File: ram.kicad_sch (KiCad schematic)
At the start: 24 parts, among them U16 SIMM, U17 74LS08, U18 74LS74, U19 74F00, U32 74LS139, U34 74LS244, U35 74LS244

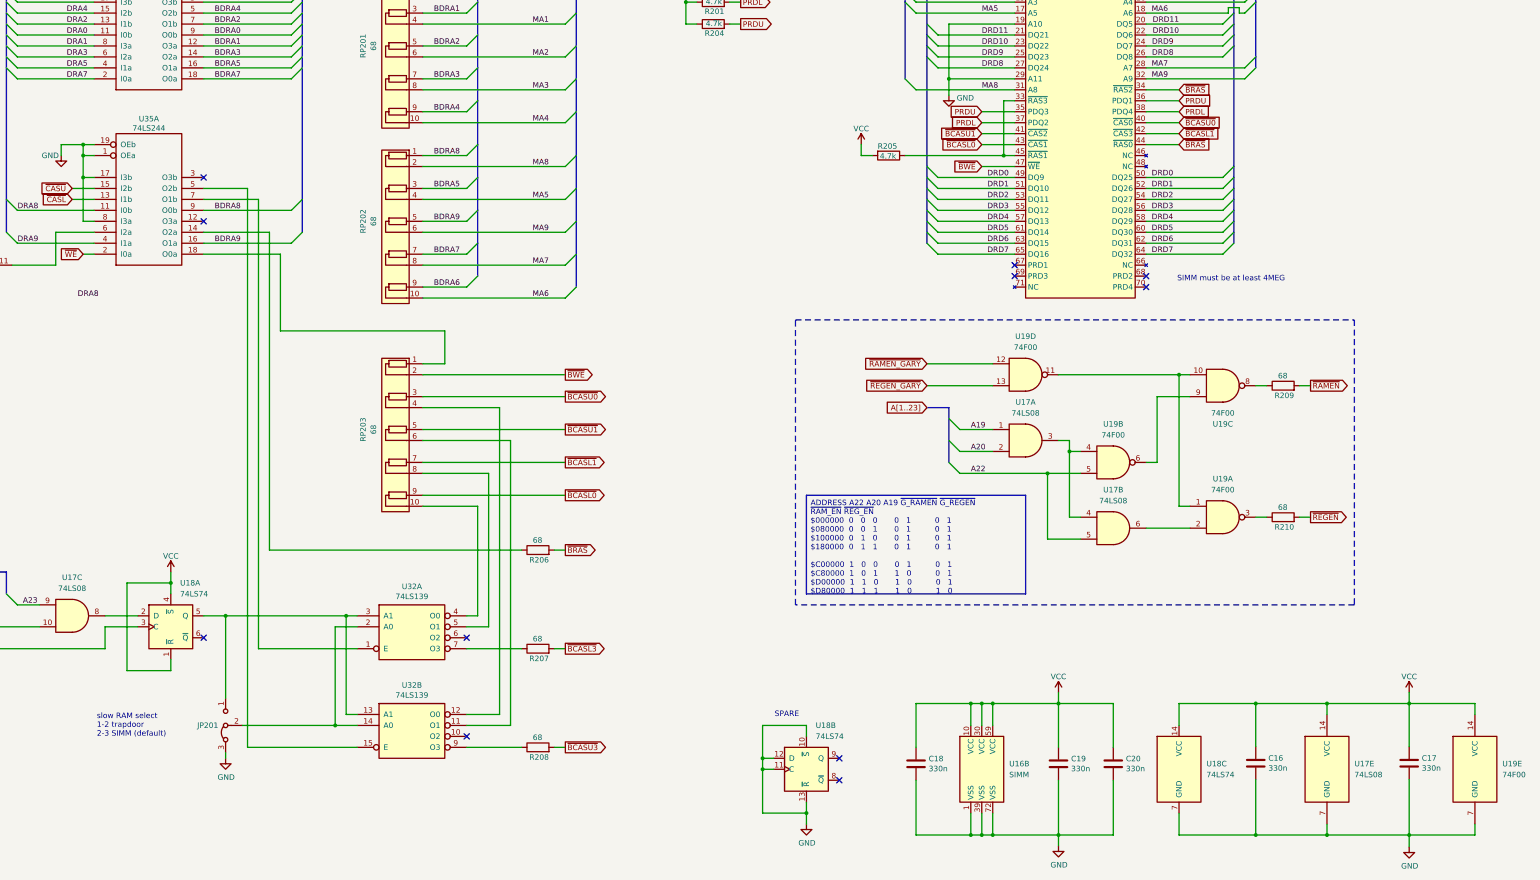
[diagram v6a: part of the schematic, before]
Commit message: Completed routing, no DRC errors (but still a lot of warnings)
TODO: thoroughly review all small schematic changes
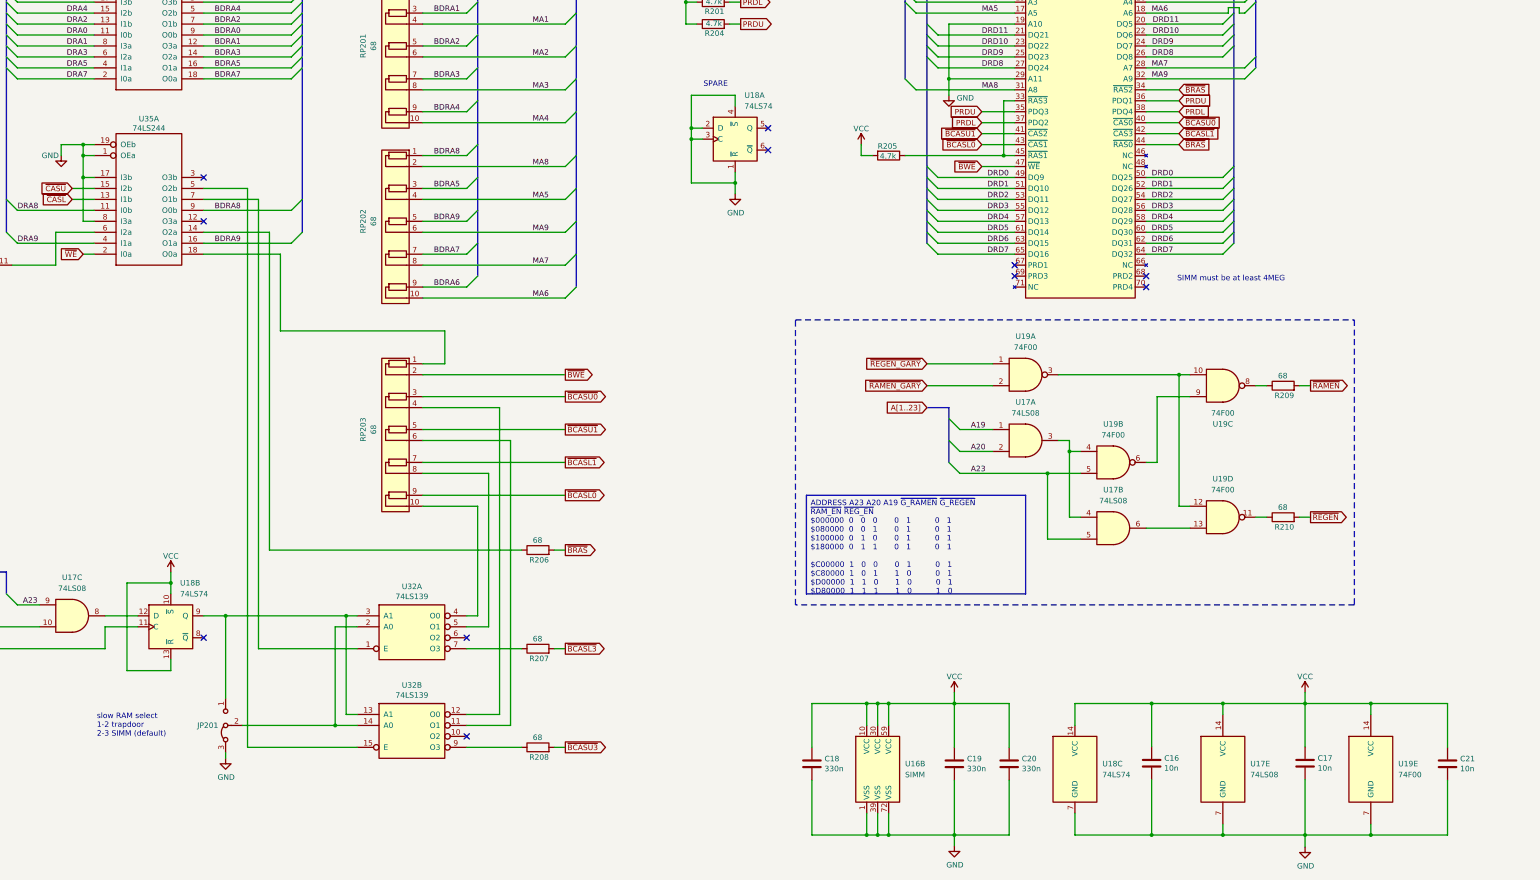
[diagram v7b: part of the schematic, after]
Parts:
- added C21: 10n, Raemixx500:C_Axial_L6.3mm_D2.5mm_P10.16mm, symbol Device:C
- C16, C17: value 330n -> 10n
- JP201: now left out of the parts list
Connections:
- net A22 is gone; now on net A23: U17.5, U19.5
- net CCKQ: now also U18.11 (C); no longer U18.3 (C)
- net GND: now also U18.1 (~{R}), U18.2 (D), U18.3 (C), U18.4 (~{S}), C21.2; no longer U18.10 (~{S}), U18.11 (C), U18.12 (D), U18.13 (~{R})
- net VCC: now also U18.10 (~{S}), U18.13 (~{R}), C21.1; no longer U18.1 (~{R}), U18.4 (~{S})
- net ~{RAMEN_GARY}: now also U19.2; no longer U19.12
- net ~{REGEN_GARY}: now also U19.1; no longer U19.13
- net at JP201.1 (A), U32.13 (A1), U32.3 (A1): now also U18.9 (Q); no longer U18.5 (Q)
- net at U17.6: now also U19.13; no longer U19.2
- net at U19.3: now also U19.10, U19.12; no longer R210.1
- net at U17.8: now also U18.12 (D); no longer U18.2 (D)
- new net: R210.1, U19.11
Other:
- moved on the sheet: C16, C17, C18, C19, C20, U16B, U17E, U18A, U18B, U18C, U19A, U19D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

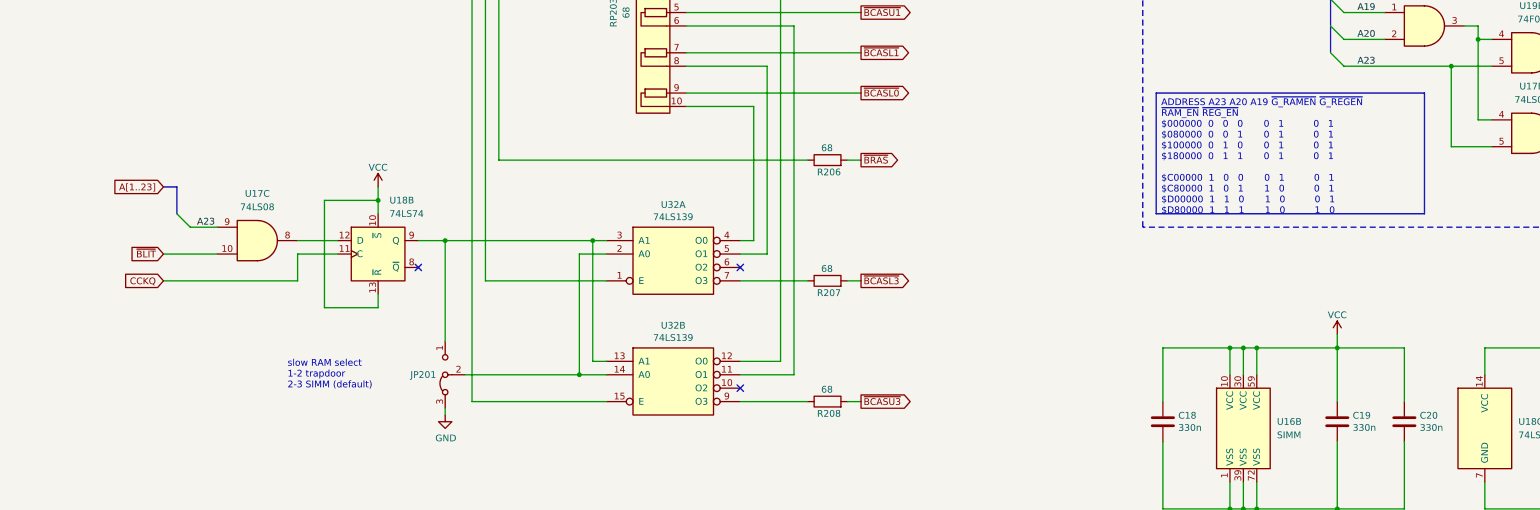
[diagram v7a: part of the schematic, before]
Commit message: fixed bug in CAS multiplexer
added logo
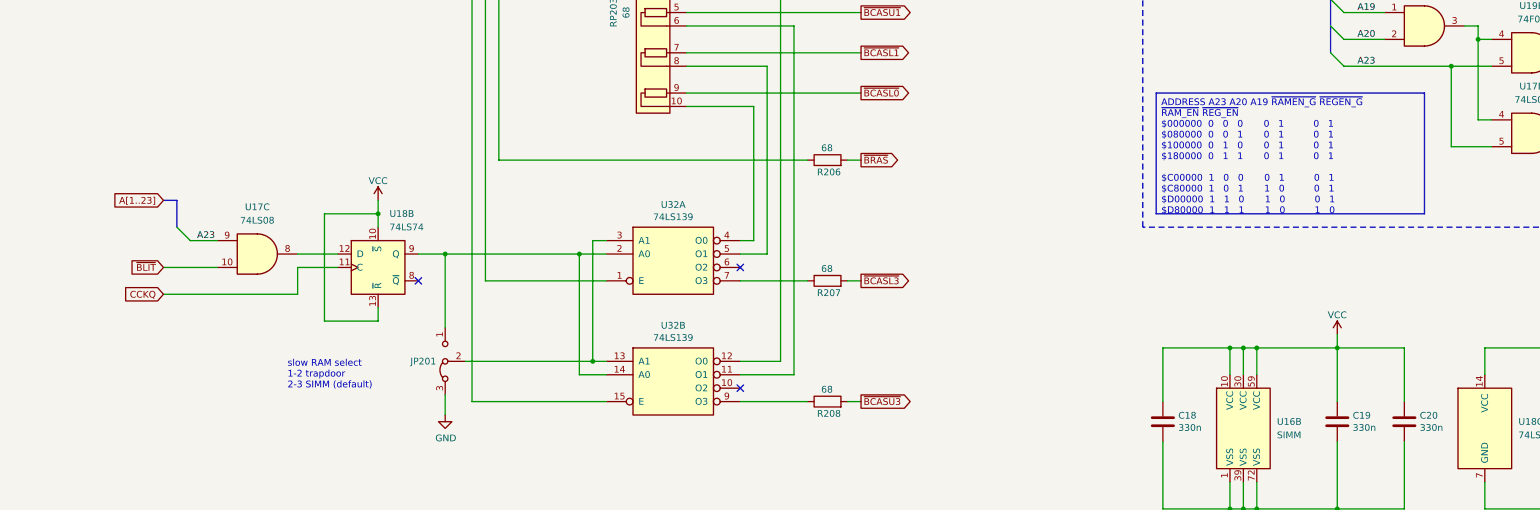
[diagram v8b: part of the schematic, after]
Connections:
- net at U32.14 (A0), U32.2 (A0): now also JP201.1 (A), U18.9 (Q); no longer JP201.2 (C)
- net at U32.13 (A1), U32.3 (A1): now also JP201.2 (C); no longer JP201.1 (A), U18.9 (Q)
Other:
- moved on the sheet: JP201, U17C, U18B
